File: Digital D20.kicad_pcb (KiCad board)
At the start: 6 copper layers, 49.5 x 49.1 mm, 14 parts

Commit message: Add 'jlcjlcjlcjlc' to mark order number placement.
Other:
- board text added: "JLCJLCJLCJLC"
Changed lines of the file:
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@@
     (effects (font (size 6 6) (thickness 0.75)))
+  )
+  (gr_text "JLCJLCJLCJLC" (at 167.894 128.778) (layer "F.SilkS")
+    (effects (font (size 1 1) (thickness 0.15)) (justify left bottom))
   )
   (gr_text "20" (at 141.990887 134.188522 60) (layer "F.Mask")

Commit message: The test board I ordered
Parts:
- removed mouse-bite-2.54mm-slot (x5): VAL**, Panelization:mouse-bite-2.54mm-slot
- moved G*** 1.76 mm to (159.7, 135.9)
- moved G*** 1.76 mm to (151.2, 137.5)
- moved G*** 1.76 mm to (158.7, 143.4)
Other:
- board size 49.5 x 49.1 mm -> 49.5 x 47 mm

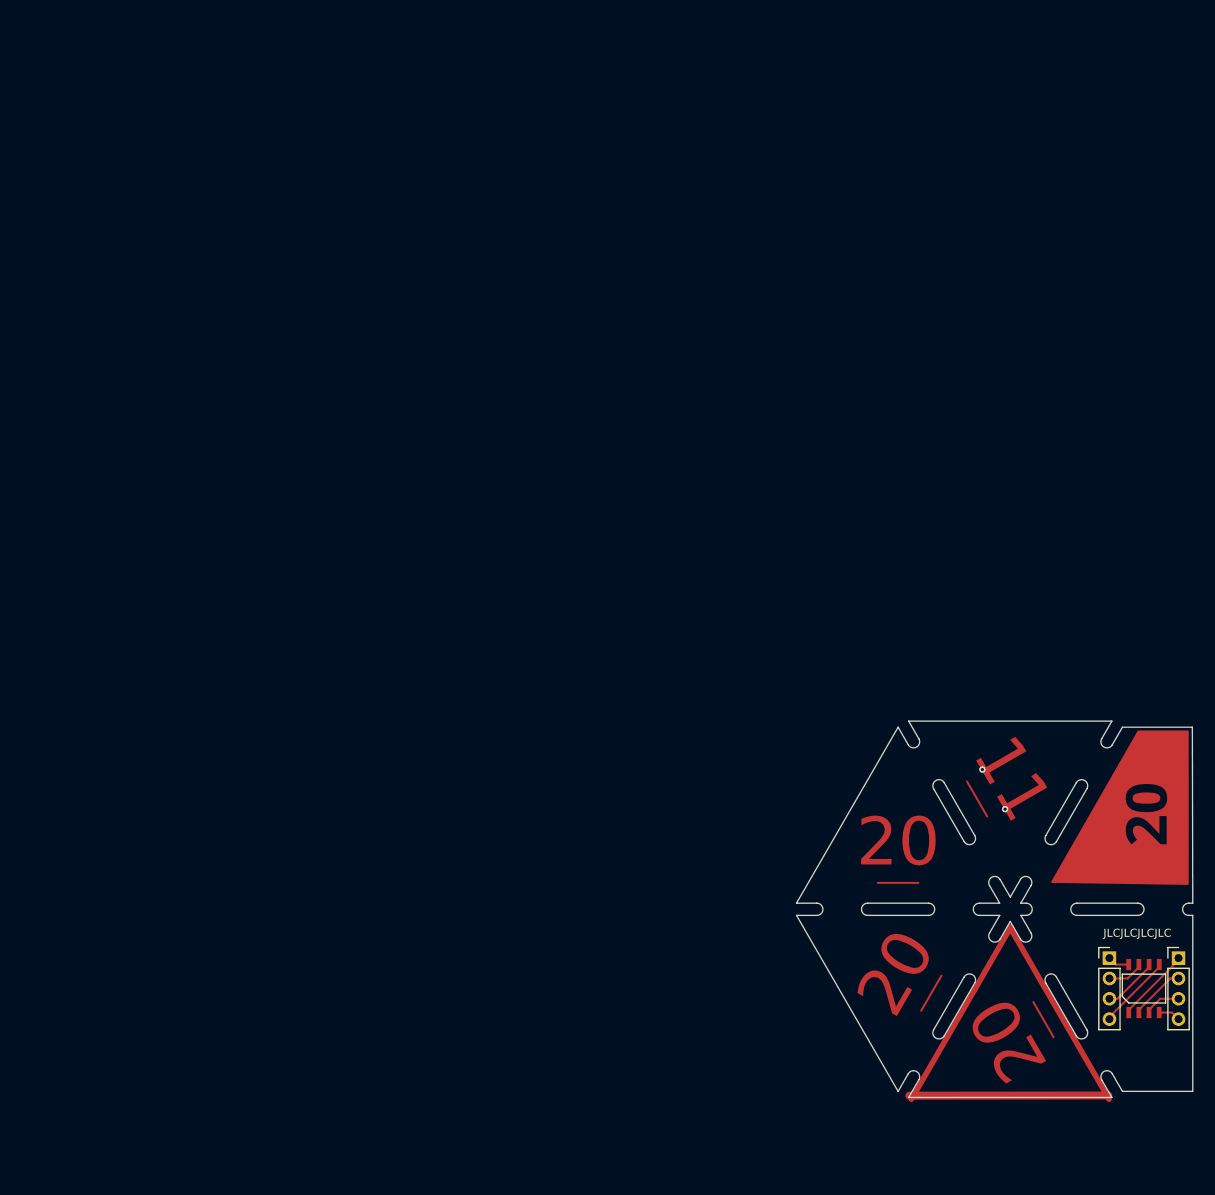
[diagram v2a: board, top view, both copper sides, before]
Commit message: Tiles rev 1. would like to tweak the lightning bolts, and doonce again try to get a nice back copper pour. Might not happen.
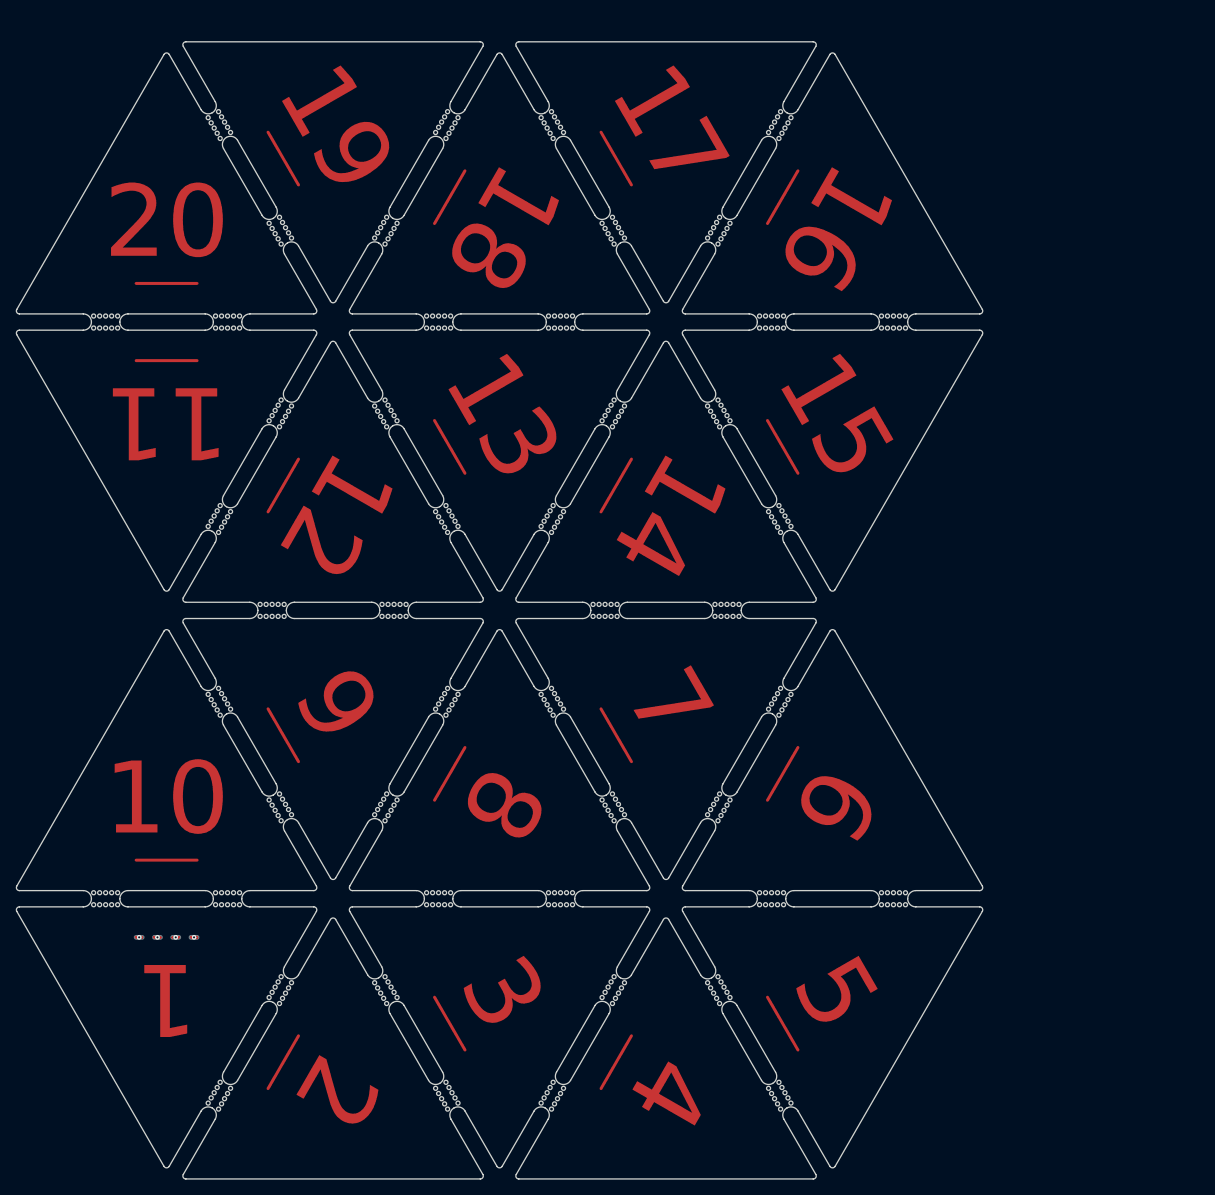
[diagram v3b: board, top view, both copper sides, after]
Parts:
- removed the G*** at (159.7, 135.9)
- removed the G*** at (148.1, 115.5)
- removed the G*** at (151.2, 137.5)
- removed the G*** at (144.7, 121.9)
- removed the G*** at (158.7, 143.4)
- removed the G*** at (134.3, 116.9)
- removed REF** (x2): PinHeader_1x04_P2.54mm_Vertical, Connector_PinHeader_2.54mm:PinHeader_1x04_P2.54mm_Vertical
- removed REF**: SOIC-8 4.9x6, random testing:SOIC-8 4.9x6
- added G***: LOGO, random testing:lightningBolt45mm, F.Cu at (66.1, 89.1)
- added G***: LOGO, random testing:lightningBolt45mm, F.Cu at (87.0, 125.1)
- added G***: LOGO, random testing:lightningBolt45mm, F.Cu at (42.2, 66.3)
- added G***: LOGO, random testing:lightningBolt45mm, F.Cu at (109.0, 34.4)
- added G***: LOGO, random testing:lightningBolt45mm, F.Cu at (111.0, 156.6)
- added G***: LOGO, random testing:lightningBolt45mm, F.Cu at (78.0, 34.0)
- added G***: LOGO, random testing:lightningBolt45mm, F.Cu at (66.1, 17.0)
- added G***: LOGO, random testing:lightningBolt45mm, F.Cu at (105.4, 75.5)
- added G***: LOGO, random testing:lightningBolt45mm, F.Cu at (78.0, 106.1)
- added G***: LOGO, random testing:lightningBolt45mm, F.Cu at (131.8, 48.5)
- added G***: LOGO, random testing:lightningBolt45mm, F.Cu at (109.0, 106.5)
- added G***: LOGO, random testing:lightningBolt45mm, F.Cu at (59.4, 37.4)
- added G***: LOGO, random testing:lightningBolt45mm, F.Cu at (69.4, 156.6)
- added G***: LOGO, random testing:lightningBolt45mm, F.Cu at (129.8, 142.6)
- added G***: LOGO, random testing:lightningBolt45mm, F.Cu at (88.2, 70.5)
- added G***: LOGO, random testing:lightningBolt45mm, F.Cu at (38.7, 111.2)
- added G***: LOGO, random testing:lightningBolt45mm, F.Cu at (99.0, 101.8)
- added G***: LOGO, random testing:lightningBolt45mm, F.Cu at (131.8, 120.5)
- added G***: LOGO, random testing:lightningBolt45mm, F.Cu at (140.4, 142.2)
- added G***: LOGO, random testing:lightningBolt45mm, F.Cu at (128.6, 125.1)
- added G***: LOGO, random testing:lightningBolt45mm, F.Cu at (98.8, 142.2)
- added G***: LOGO, random testing:lightningBolt45mm, F.Cu at (87.0, 53.0)
- added G***: LOGO, random testing:lightningBolt45mm, F.Cu at (98.8, 70.1)
- added G***: LOGO, random testing:lightningBolt45mm, F.Cu at (63.7, 147.6)
- added G***: LOGO, random testing:lightningBolt45mm, F.Cu at (62.9, 136.6)
- added G***: LOGO, random testing:lightningBolt45mm, F.Cu at (84.5, 111.6)
- added G***: LOGO, random testing:lightningBolt45mm, F.Cu at (99.0, 29.7)
- added G***: LOGO, random testing:lightningBolt45mm, F.Cu at (47.1, 128.9)
- added G***: LOGO, random testing:lightningBolt45mm, F.Cu at (105.4, 147.6)
- added G***: LOGO, random testing:lightningBolt45mm, F.Cu at (69.4, 84.5)
- added G***: LOGO, random testing:lightningBolt45mm, F.Cu at (107.8, 89.1)
- added G***: LOGO, random testing:lightningBolt45mm, F.Cu at (111.0, 84.5)
- added G***: LOGO, random testing:lightningBolt45mm, F.Cu at (62.9, 64.5)
- added G***: LOGO, random testing:lightningBolt45mm, F.Cu at (78.2, 65.7)
- added G***: LOGO, random testing:lightningBolt45mm, F.Cu at (84.5, 39.5)
- added G***: LOGO, random testing:lightningBolt45mm, F.Cu at (126.2, 39.5)
- added G***: LOGO, random testing:lightningBolt45mm, F.Cu at (129.8, 70.5)
- added G***: LOGO, random testing:lightningBolt45mm, F.Cu at (128.6, 53.0)
- added G***: LOGO, random testing:lightningBolt45mm, F.Cu at (54.5, 118.9)
- added G***: LOGO, random testing:lightningBolt45mm, F.Cu at (38.7, 39.1)
- added G***: LOGO, random testing:lightningBolt45mm, F.Cu at (90.2, 120.5)
- added G***: LOGO, random testing:lightningBolt45mm, F.Cu at (54.5, 46.8)
- added G***: LOGO, random testing:lightningBolt45mm, F.Cu at (119.9, 65.7)
- added G***: LOGO, random testing:lightningBolt45mm, F.Cu at (119.9, 137.8)
- added G***: LOGO, random testing:lightningBolt45mm, F.Cu at (140.7, 101.8)
- added G***: LOGO, random testing:lightningBolt45mm, F.Cu at (119.6, 34.0)
- added G***: LOGO, random testing:lightningBolt45mm, F.Cu at (119.6, 106.1)
- added G***: LOGO, random testing:lightningBolt45mm, F.Cu at (88.2, 142.6)
- added G***: LOGO, random testing:lightningBolt45mm, F.Cu at (107.8, 17.0)
- added G***: LOGO, random testing:lightningBolt45mm, F.Cu at (47.1, 56.8)
- added G***: LOGO, random testing:lightningBolt45mm, F.Cu at (90.2, 48.5)
- added G***: LOGO, random testing:lightningBolt45mm, F.Cu at (42.2, 138.3)
- added G***: LOGO, random testing:lightningBolt45mm, F.Cu at (140.4, 70.1)
- added G***: LOGO, random testing:lightningBolt45mm, F.Cu at (59.4, 109.5)
- added G***: LOGO, random testing:lightningBolt45mm, F.Cu at (140.7, 29.7)
- added G***: LOGO, random testing:lightningBolt45mm, F.Cu at (63.7, 75.5)
- added G***: LOGO, random testing:lightningBolt45mm, F.Cu at (67.4, 34.4)
- added G***: LOGO, random testing:lightningBolt45mm, F.Cu at (78.2, 137.8)
- added G***: LOGO, random testing:lightningBolt45mm, F.Cu at (126.2, 111.6)
- added G***: LOGO, random testing:lightningBolt45mm, F.Cu at (67.4, 106.5)
- added mouse-bite-2mm-slot (x2): VAL**, Panelization:mouse-bite-2mm-slot, F.Cu at (119.8, 112.5)
- added mouse-bite-2mm-slot (x2): VAL**, Panelization:mouse-bite-2mm-slot, F.Cu at (99.0, 148.5)
- added mouse-bite-2mm-slot (x2): VAL**, Panelization:mouse-bite-2mm-slot, F.Cu at (57.4, 27.2)
- added mouse-bite-2mm-slot (x2): VAL**, Panelization:mouse-bite-2mm-slot, F.Cu at (127.4, 99.3)
- added mouse-bite-2mm-slot (x2): VAL**, Panelization:mouse-bite-2mm-slot, F.Cu at (99.0, 76.4)
- added mouse-bite-2mm-slot (x2): VAL**, Panelization:mouse-bite-2mm-slot, F.Cu at (127.4, 148.5)
- added mouse-bite-2mm-slot (x2): VAL**, Panelization:mouse-bite-2mm-slot, F.Cu at (141.7, 123.9)
- added mouse-bite-2mm-slot (x2): VAL**, Panelization:mouse-bite-2mm-slot, F.Cu at (99.0, 27.2)
- added mouse-bite-2mm-slot (x2): VAL**, Panelization:mouse-bite-2mm-slot, F.Cu at (105.6, 87.9)
- added mouse-bite-2mm-slot (x2): VAL**, Panelization:mouse-bite-2mm-slot, F.Cu at (85.8, 148.5)
- added mouse-bite-2mm-slot (x2): VAL**, Panelization:mouse-bite-2mm-slot, F.Cu at (57.4, 76.4)
- added mouse-bite-2mm-slot (x2): VAL**, Panelization:mouse-bite-2mm-slot, F.Cu at (85.8, 27.2)
- added mouse-bite-2mm-slot (x2): VAL**, Panelization:mouse-bite-2mm-slot, F.Cu at (58.4, 51.8)
- added mouse-bite-2mm-slot (x2): VAL**, Panelization:mouse-bite-2mm-slot, F.Cu at (120.8, 87.9)
- added mouse-bite-2mm-slot (x2): VAL**, Panelization:mouse-bite-2mm-slot, F.Cu at (106.6, 40.4)
- added mouse-bite-2mm-slot (x2): VAL**, Panelization:mouse-bite-2mm-slot, F.Cu at (127.4, 27.2)
- added mouse-bite-2mm-slot (x2): VAL**, Panelization:mouse-bite-2mm-slot, F.Cu at (127.4, 76.4)
- added mouse-bite-2mm-slot (x2): VAL**, Panelization:mouse-bite-2mm-slot, F.Cu at (100.0, 51.8)
- added mouse-bite-2mm-slot (x2): VAL**, Panelization:mouse-bite-2mm-slot, F.Cu at (65.0, 112.5)
- added mouse-bite-2mm-slot (x2): VAL**, Panelization:mouse-bite-2mm-slot, F.Cu at (126.4, 123.9)
- added mouse-bite-2mm-slot (x2): VAL**, Panelization:mouse-bite-2mm-slot, F.Cu at (65.0, 63.2)
- added mouse-bite-2mm-slot (x2): VAL**, Panelization:mouse-bite-2mm-slot, F.Cu at (106.6, 112.5)
- added mouse-bite-2mm-slot (x2): VAL**, Panelization:mouse-bite-2mm-slot, F.Cu at (78.2, 40.4)
- added mouse-bite-2mm-slot (x2): VAL**, Panelization:mouse-bite-2mm-slot, F.Cu at (106.6, 135.3)
- added mouse-bite-2mm-slot (x2): VAL**, Panelization:mouse-bite-2mm-slot, F.Cu at (141.7, 51.8)
- added mouse-bite-2mm-slot (x2): VAL**, Panelization:mouse-bite-2mm-slot, F.Cu at (57.4, 99.3)
- added mouse-bite-2mm-slot (x2): VAL**, Panelization:mouse-bite-2mm-slot, F.Cu at (119.8, 135.3)
- added mouse-bite-2mm-slot (x2): VAL**, Panelization:mouse-bite-2mm-slot, F.Cu at (43.2, 123.9)
- added mouse-bite-2mm-slot (x2): VAL**, Panelization:mouse-bite-2mm-slot, F.Cu at (119.8, 40.4)
- added mouse-bite-2mm-slot (x2): VAL**, Panelization:mouse-bite-2mm-slot, F.Cu at (119.8, 63.2)
- added mouse-bite-2mm-slot (x2): VAL**, Panelization:mouse-bite-2mm-slot, F.Cu at (84.8, 123.9)
- added mouse-bite-2mm-slot (x2): VAL**, Panelization:mouse-bite-2mm-slot, F.Cu at (78.2, 135.3)
- added mouse-bite-2mm-slot (x2): VAL**, Panelization:mouse-bite-2mm-slot, F.Cu at (99.0, 99.3)
- added mouse-bite-2mm-slot (x2): VAL**, Panelization:mouse-bite-2mm-slot, F.Cu at (64.0, 87.9)
- added mouse-bite-2mm-slot (x2): VAL**, Panelization:mouse-bite-2mm-slot, F.Cu at (85.8, 99.3)
- added mouse-bite-2mm-slot (x2): VAL**, Panelization:mouse-bite-2mm-slot, F.Cu at (84.8, 51.8)
- added mouse-bite-2mm-slot (x2): VAL**, Panelization:mouse-bite-2mm-slot, F.Cu at (85.8, 76.4)
- added mouse-bite-2mm-slot (x2): VAL**, Panelization:mouse-bite-2mm-slot, F.Cu at (78.2, 63.2)
- added mouse-bite-2mm-slot (x2): VAL**, Panelization:mouse-bite-2mm-slot, F.Cu at (79.2, 87.9)
- added mouse-bite-2mm-slot (x2): VAL**, Panelization:mouse-bite-2mm-slot, F.Cu at (106.6, 63.2)
- added mouse-bite-2mm-slot (x2): VAL**, Panelization:mouse-bite-2mm-slot, F.Cu at (78.2, 112.5)
- added mouse-bite-2mm-slot (x2): VAL**, Panelization:mouse-bite-2mm-slot, F.Cu at (43.2, 51.8)
- added mouse-bite-2mm-slot (x2): VAL**, Panelization:mouse-bite-2mm-slot, F.Cu at (126.4, 51.8)
- added mouse-bite-2mm-slot (x2): VAL**, Panelization:mouse-bite-2mm-slot, F.Cu at (65.0, 40.4)
- added mouse-bite-2mm-slot (x2): VAL**, Panelization:mouse-bite-2mm-slot, F.Cu at (57.4, 148.5)
- added mouse-bite-2mm-slot (x2): VAL**, Panelization:mouse-bite-2mm-slot, F.Cu at (58.4, 123.9)
- added mouse-bite-2mm-slot (x2): VAL**, Panelization:mouse-bite-2mm-slot, F.Cu at (100.0, 123.9)
- added mouse-bite-2mm-slot (x2): VAL**, Panelization:mouse-bite-2mm-slot, F.Cu at (65.0, 135.3)
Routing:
- net (no net): track 47.3 -> 0.00 mm, vias 2 -> 4
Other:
- board size 49.5 x 47 mm -> 120.8 x 142.1 mm
- board text added: "1"
- board text added: "10"
- board text added: "12"
- board text added: "13"
- board text added: "14"
- board text added: "15"
- board text added: "16"
- board text added: "17"
- board text added: "18"
- board text added: "19"
- board text added: "2"
- board text added: "3"
- board text added: "4"
- board text added: "5"
- board text added: "6"
- board text added: "7"
- board text added: "8"
- board text added: "9"
- board text removed: "JLCJLCJLCJLC"

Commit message: Tiles rev 1 with test gerbers.
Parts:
- added ?: , , F.Cu at (146.9, 64.2)
- added ?: , , F.Cu at (148.2, 110.8)
- added ?: , , F.Cu at (149.3, 63.0)
- added ?: , , F.Cu at (139.6, 76.7)
- added ?: , , F.Cu at (148.0, 113.5)
- added ?: , , F.Cu at (140.7, 101.0)
- added ?: , , F.Cu at (142.0, 75.5)
- added ?: , , F.Cu at (140.9, 98.3)
- added mouse-bite-2mm-slot (x2): VAL**, Panelization:mouse-bite-2mm-slot, F.Cu at (140.6, 99.3)
- added mouse-bite-2mm-slot (x2): VAL**, Panelization:mouse-bite-2mm-slot, F.Cu at (148.3, 112.5)
- added mouse-bite-2mm-slot (x2): VAL**, Panelization:mouse-bite-2mm-slot, F.Cu at (148.3, 63.2)
- added mouse-bite-2mm-slot (x2): VAL**, Panelization:mouse-bite-2mm-slot, F.Cu at (140.6, 76.4)
- moved G*** 1.62 mm to (87.4, 54.6), turned to -65 degrees
- moved G*** 1.62 mm to (77.0, 138.9)
- moved G*** 1.61 mm to (118.3, 137.3)
- moved G*** 1.36 mm to (78.9, 107.1)
- moved G*** 1.01 mm to (69.4, 157.6)
- moved G*** 0.92 mm to (108.5, 89.6)
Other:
- outline, holes or cut-outs redrawn
- board text added: "JLCJLCJLCJLC"

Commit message: switch to 4 groups of boards?
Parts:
- removed ? (x8): , 
- removed the mouse-bite-2mm-slot at (140.6, 99.3) (x2)
- removed the mouse-bite-2mm-slot at (65.0, 63.2) (x2)
- removed the mouse-bite-2mm-slot at (78.2, 40.4) (x2)
- removed the mouse-bite-2mm-slot at (119.8, 40.4) (x2)
- removed the mouse-bite-2mm-slot at (78.2, 63.2) (x2)
- removed the mouse-bite-2mm-slot at (119.8, 63.2) (x2)
- removed the mouse-bite-2mm-slot at (99.0, 148.5) (x2)
- removed the mouse-bite-2mm-slot at (57.4, 27.2) (x2)
- removed the mouse-bite-2mm-slot at (127.4, 99.3) (x2)
- removed the mouse-bite-2mm-slot at (99.0, 76.4) (x2)
- removed the mouse-bite-2mm-slot at (127.4, 148.5) (x2)
- removed the mouse-bite-2mm-slot at (99.0, 27.2) (x2)
- removed the mouse-bite-2mm-slot at (119.8, 112.5) (x2)
- removed the mouse-bite-2mm-slot at (85.8, 148.5) (x2)
- removed the mouse-bite-2mm-slot at (57.4, 76.4) (x2)
- removed the mouse-bite-2mm-slot at (106.6, 40.4) (x2)
- removed the mouse-bite-2mm-slot at (127.4, 27.2) (x2)
- removed the mouse-bite-2mm-slot at (127.4, 76.4) (x2)
- removed the mouse-bite-2mm-slot at (85.8, 27.2) (x2)
- removed the mouse-bite-2mm-slot at (65.0, 112.5) (x2)
- removed the mouse-bite-2mm-slot at (106.6, 112.5) (x2)
- removed the mouse-bite-2mm-slot at (106.6, 135.3) (x2)
- removed the mouse-bite-2mm-slot at (57.4, 99.3) (x2)
- removed the mouse-bite-2mm-slot at (119.8, 135.3) (x2)
- removed the mouse-bite-2mm-slot at (78.2, 135.3) (x2)
- removed the mouse-bite-2mm-slot at (85.8, 99.3) (x2)
- removed the mouse-bite-2mm-slot at (148.3, 112.5) (x2)
- removed the mouse-bite-2mm-slot at (85.8, 76.4) (x2)
- removed the mouse-bite-2mm-slot at (99.0, 99.3) (x2)
- removed the mouse-bite-2mm-slot at (78.2, 112.5) (x2)
- removed the mouse-bite-2mm-slot at (148.3, 63.2) (x2)
- removed the mouse-bite-2mm-slot at (140.6, 76.4) (x2)
- removed the mouse-bite-2mm-slot at (65.0, 40.4) (x2)
- removed the mouse-bite-2mm-slot at (57.4, 148.5) (x2)
- removed the mouse-bite-2mm-slot at (106.6, 63.2) (x2)
- removed the mouse-bite-2mm-slot at (65.0, 135.3) (x2)
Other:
- outline, holes or cut-outs redrawn
